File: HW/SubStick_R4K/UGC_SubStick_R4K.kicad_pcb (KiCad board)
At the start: 2 copper layers, 50.1 x 31 mm, 7 parts, among them J1 Conn_01x06_Pin, J2 503480-0640, SW1 GL18_SW

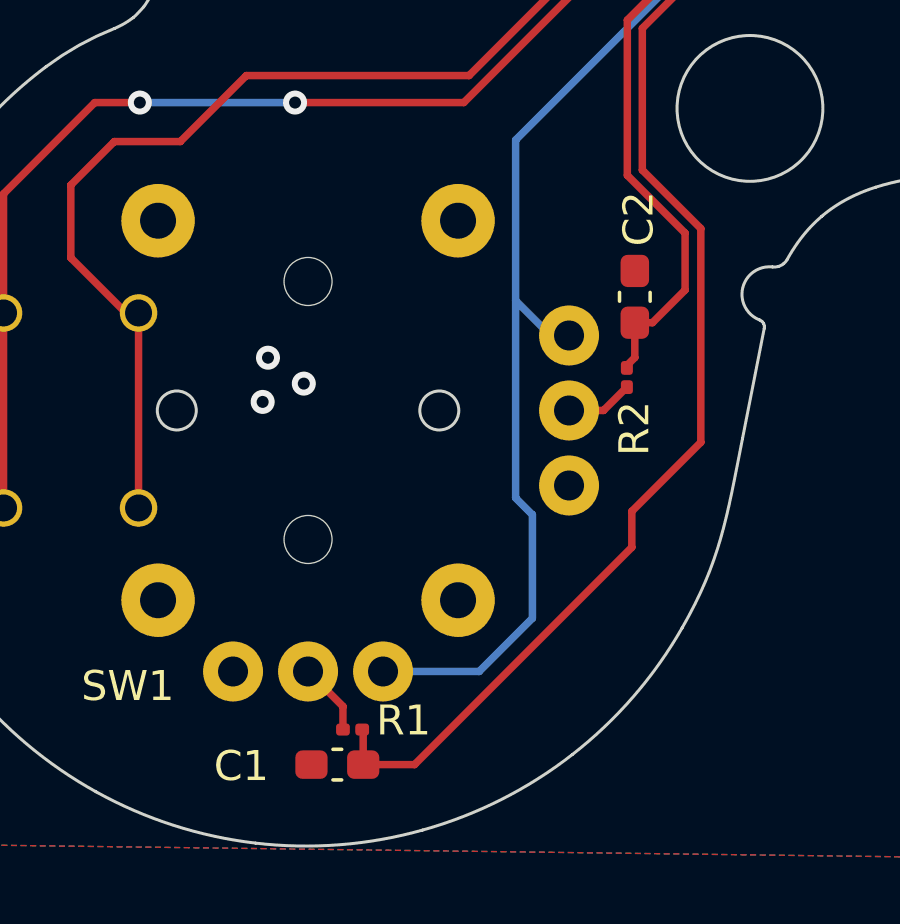
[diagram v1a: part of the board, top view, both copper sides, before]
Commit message: Update PCBs
- Fix BOMs so they reference real part numbers
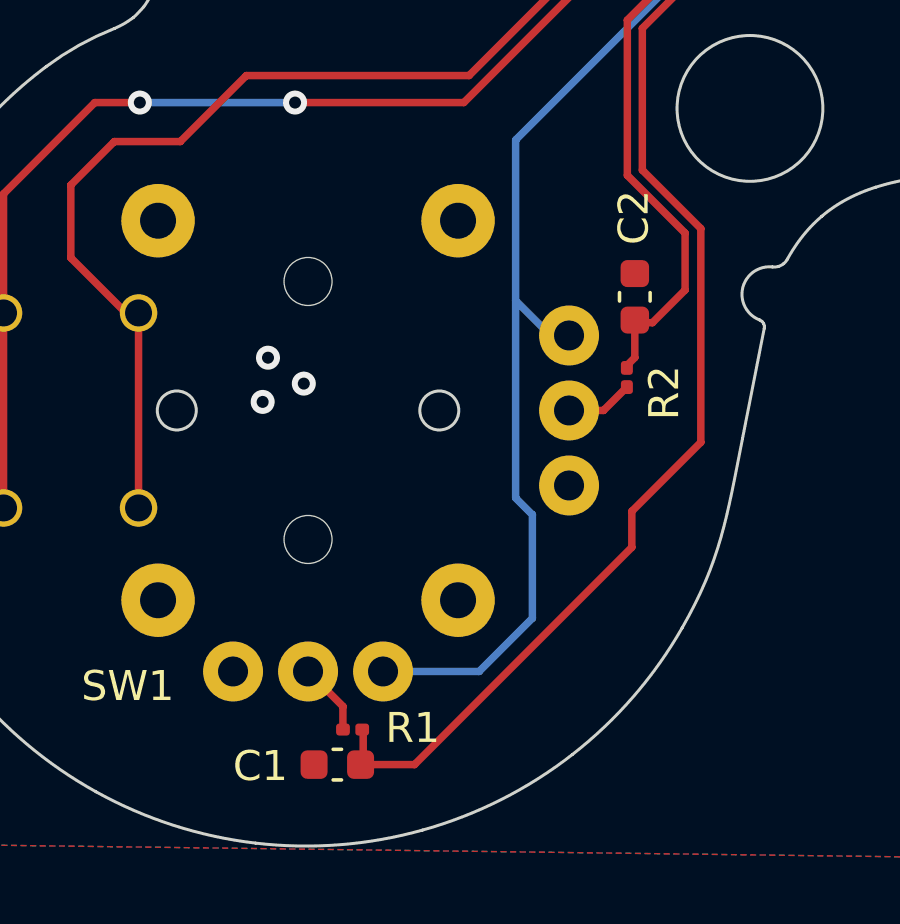
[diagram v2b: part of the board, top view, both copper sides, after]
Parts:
- C1, C2: value .047u -> 47nF; footprint Capacitor_SMD:C_0603_1608Metric_Pad1.08x0.95mm_HandSolder -> Capacitor_SMD:C_0603_1608Metric
